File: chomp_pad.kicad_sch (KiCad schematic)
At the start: 94 parts, among them J1 SJ-43514, J2 LED, J3 OLED, SW1 SW_PUSH, SW10 SW_PUSH, SW11 SW_PUSH, SW12 SW_PUSH, SW13 SW_PUSH, SW14 SW_PUSH, SW15 SW_PUSH, SW16 SW_PUSH, SW17 SW_PUSH, SW18 SW_PUSH, SW19 SW_PUSH, SW2 SW_PUSH, SW20 SW_PUSH, SW21 SW_PUSH, SW22 SW_PUSH, SW23 SW_PUSH, SW24 SW_PUSH, SW25 SW_PUSH, SW26 SW_PUSH, SW27 SW_PUSH, SW3 SW_PUSH, SW4 SW_PUSH, SW5 SW_PUSH, SW6 SW_PUSH, SW7 SW_PUSH, SW8 SW_PUSH, SW9 SW_PUSH, U1 kbd:ProMicro

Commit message: getting started
starting PCB
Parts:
- SW27: footprint kbd:MX_ALPS_PG1350_noLed -> (none)
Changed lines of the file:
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@@
     (property "Reference" "SW27" (id 0) (at 243.84 78.486 0))
     (property "Value" "SW_PUSH" (id 1) (at 240.03 83.312 0))
-    (property "Footprint" "kbd:MX_ALPS_PG1350_noLed" (id 2) (at 240.03 81.28 0)
+    (property "Footprint" "" (id 2) (at 240.03 81.28 0)
       (effects (font (size 1.27 1.27)) hide)
     )
@@
     )
     (path "/a63de8d8-556e-460c-b1fe-c7ccba6e59e8"
-      (reference "SW27") (unit 1) (value "SW_PUSH") (footprint "kbd:MX_ALPS_PG1350_noLed")
+      (reference "SW27") (unit 1) (value "SW_PUSH") (footprint "kbd:MX_ALPS_PG1350_noLed_1.75u")
     )
     (path "/71e46ee0-ea70-461a-85e4-97485bdc2a73"

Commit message: sleepy
did a lot, need to fix dependencies on footprints but too lazy to
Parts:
- added D28: D, kbd:D3_TH_SMD, symbol lets_split-rescue:D
- added SW28: Rotary_Encoder_Switch, SofleKeyboard-footprint:RotaryEncoder_Alps_EC11E-Switch_Vertical_H20mm-keebio_modified, symbol Device:Rotary_Encoder_Switch
- SW1, SW10, SW11, SW12, SW13, SW14, SW15, SW16, SW17, SW18, SW19, SW2, SW20, SW21, SW22, SW23, SW24, SW25, SW26, SW3, SW4, SW5, SW6, SW7, SW8, SW9: footprint kbd:MX_ALPS_PG1350_noLed -> (none)
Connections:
- net GND: now also SW28.C
- net row4: now also D28.1 (K)
- net ENCB: now reaches U1.13 (B6/10)
- net ENCB: now also SW28.B
- net ENCA: now reaches U1.14 (B2/16)
- net ENCA: now also SW28.A
- net col0 renamed SW28A
- net SW28A: now also SW28.S1
- new net SW28B: D28.2 (A), SW28.S2
- no-connect marks 6 -> 4

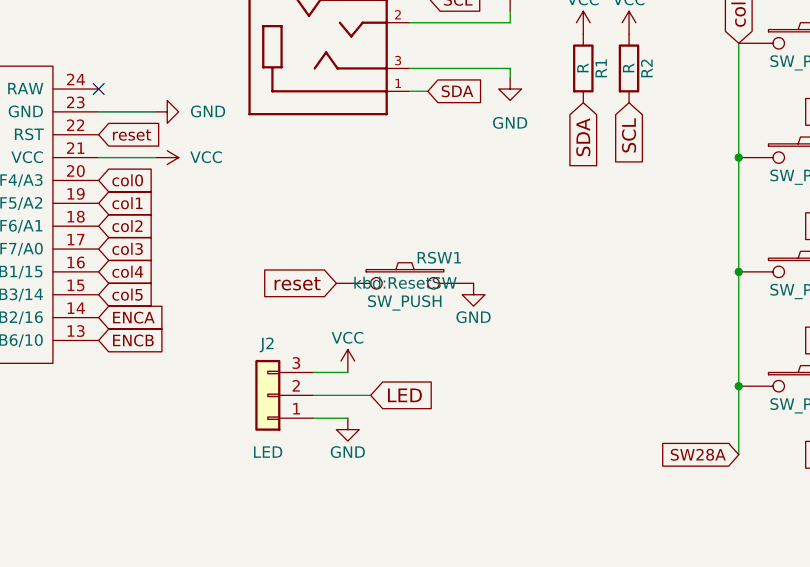
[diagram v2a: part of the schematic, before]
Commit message: fixed footprint and symbol dependencies
still need to do 3d files but screw that
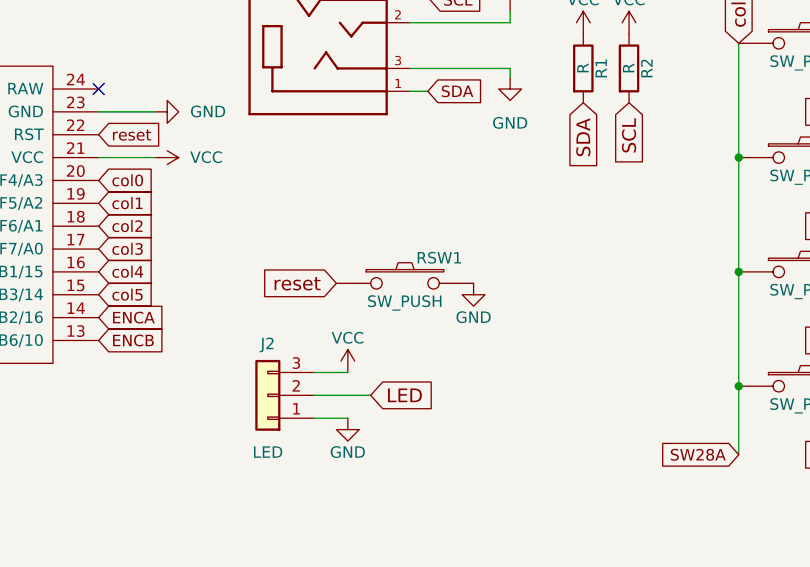
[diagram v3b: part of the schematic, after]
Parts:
- D1, D10, D11, D12, D13, D14, D15, D16, D17, D18, D19, D2, D20, D21, D22, D23, D24, D25, D26, D27, D28, D3, D4, D5, D6, D7, D8, D9: footprint kbd:D3_TH_SMD -> (none)
- J1: footprint TRRS:CUI_SJ-43514 -> (none)
- J2: footprint kbd:StripLED_rev -> (none)
- J3: footprint kbd:OLED -> (none)
- L1, L2, L3, L4, L5, L6: footprint kbd:SK6812MINI_underglow_rev -> (none)
- L10, L11, L12, L13, L14, L15, L16, L17, L18, L19, L20, L21, L22, L23, L24, L25, L26, L27, L28, L29, L30, L31, L32, L33, L7, L8, L9: footprint kbd:SK6812MINI_rev -> (none)
- R1, R2: footprint kbd:R -> (none)
- RSW1: footprint kbd:ResetSW -> (none)
- SW28: footprint SofleKeyboard-footprint:RotaryEncoder_Alps_EC11E-Switch_Vertical_H20mm-keebio_modified -> (none)
- U1: footprint kbd:ProMicro_v2 -> (none)
